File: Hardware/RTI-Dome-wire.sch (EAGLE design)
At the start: 34 parts, among them IC2 74LVC244

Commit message: Auto detect shutter presence.
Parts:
- added C5: 100nF, rti:C-EU'0805'
- added IC1: 24AA128ST, microchip:24AA128ST
- added R1, R3: 1K, rti:R-EU'0805'
- X10, X7, X9: device con-ptr500:AK500/2 -> con-ptr500:AK500/3
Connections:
- removed net 13: PCB1.13
- removed net N$6: JP4.1, PCB1.SCL1
- removed net N$8: JP4.2, PCB1.SDA1
- new net D13: PCB1.13, X8-2.KL
- new net SCL: IC1.SCL, JP4.1, PCB1.SCL1, R3.1
- new net SDA: IC1.SDA, JP4.2, PCB1.SDA1, R1.1
- net +12V: now also X11-2.KL; no longer X7-2.KL
- net 3.3V: now also C5.1, IC1.VCC, R1.2, R3.2
- net AT_PARK_PIN: now also X7-2.KL; no longer X11-1.KL
- net AT_PARK_PIN_LOOP: now also X7-3.KL; no longer X11-2.KL
- net GND: now also C5.2, IC1.A0, IC1.A1, IC1.A2, IC1.GND, X10-2.KL, X11-1.KL, X9-3.KL; no longer X10-1.KL
- net M_DIR_5V: now also X10-1.KL; no longer X9-2.KL
- net M_EN_5V: now also X9-2.KL; no longer X10-2.KL
- net M_STEP_5V: now also X10-3.KL; no longer X8-2.KL
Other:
- moved on the sheet: C1, IC2, R13, R14, R15, R16, R17, R18, R19, R4, R5, X10-1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

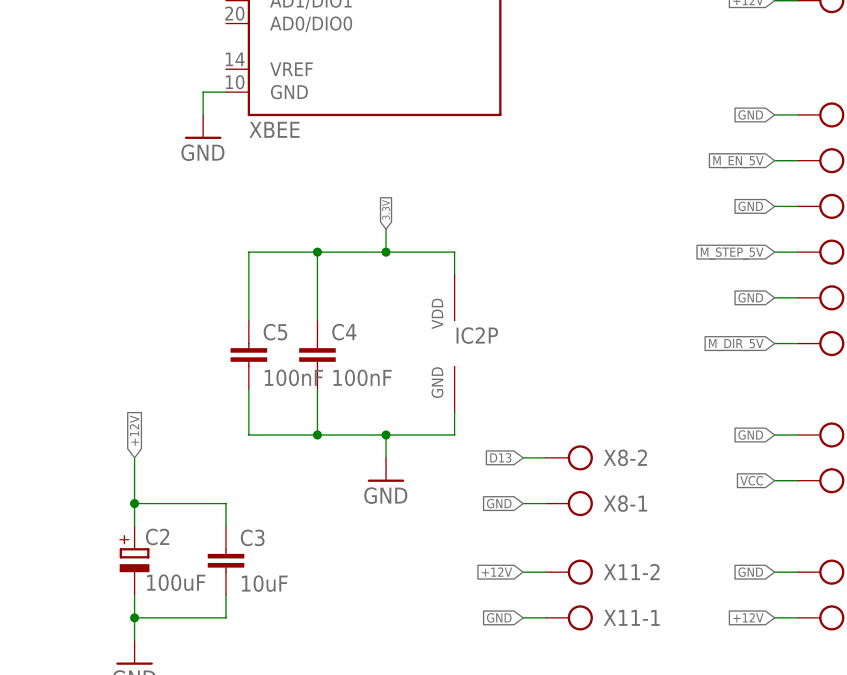
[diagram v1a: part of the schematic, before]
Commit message: Tested the ISD04 stepper controller.. needed to add 3.3V header as the pull-up on the buffer output don't bring the signal to 5V and therefore the optocoupler in the contoller doesn't do the right thing.
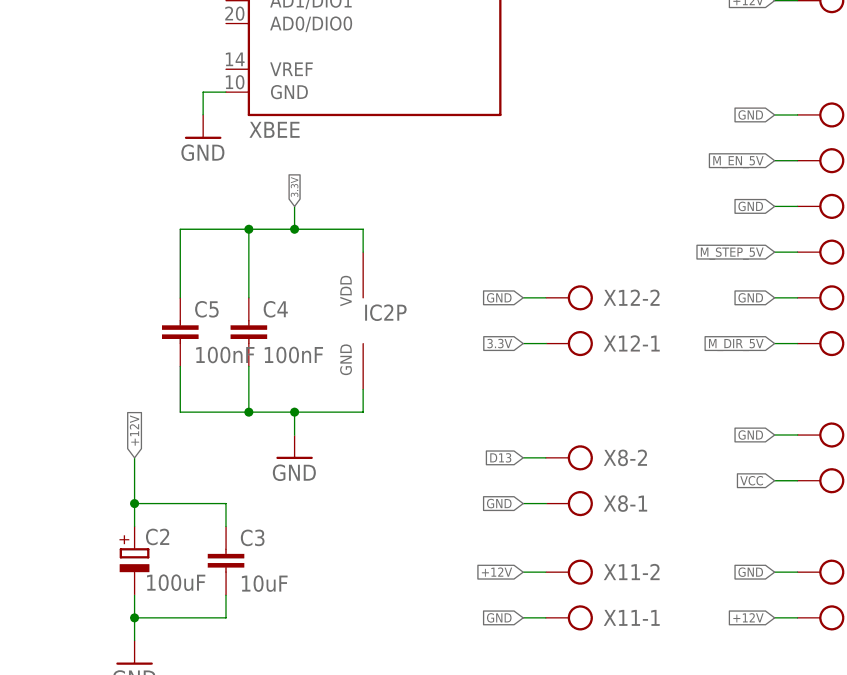
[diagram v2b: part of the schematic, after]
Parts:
- added X12: (no value), con-ptr500:AK500/2
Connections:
- net 3.3V: now also X12-1.KL
- net GND: now also X12-2.KL
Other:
- moved on the sheet: C4, C5, IC2P
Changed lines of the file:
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@@
 <part name="R3" library="rti" deviceset="R-EU" device="'0805'" value="1K"/>
 <part name="C5" library="rti" deviceset="C-EU" device="'0805'" value="100nF"/>
+<part name="X12" library="con-ptr500" deviceset="AK500/2" device=""/>
 </parts>
 <sheets>
@@
 <instance part="R8" gate="G$1" x="5.08" y="154.94" rot="R90"/>
 <instance part="R10" gate="G$1" x="5.08" y="167.64" rot="R90"/>
-<instance part="C4" gate="G$1" x="195.58" y="76.2"/>
-<instance part="IC2" gate="P" x="208.28" y="76.2" rot="R270"/>
-<instance part="GND1" gate="1" x="203.2" y="60.96"/>
+<instance part="C4" gate="G$1" x="187.96" y="78.74"/>
+<instance part="IC2" gate="P" x="198.12" y="78.74" rot="R270"/>
+<instance part="GND1" gate="1" x="193.04" y="63.5"/>
 <instance part="XB1" gate="G$1" x="200.66" y="132.08"/>
 <instance part="GND6" gate="1" x="182.88" y="99.06"/>
@@
 <instance part="R1" gate="G$1" x="73.66" y="157.48" rot="R90"/>
 <instance part="R3" gate="G$1" x="38.1" y="165.1" rot="R90"/>
-<instance part="C5" gate="G$1" x="187.96" y="76.2"/>
+<instance part="C5" gate="G$1" x="180.34" y="78.74"/>
+<instance part="X12" gate="-1" x="226.06" y="76.2" rot="R180"/>
+<instance part="X12" gate="-2" x="226.06" y="81.28" rot="R180"/>
 </instances>
 <busses>
@@
 </segment>
 <segment>
-<wire x1="195.58" y1="66.04" x2="203.2" y2="66.04" width="0.1524" layer="91"/>
-<wire x1="203.2" y1="66.04" x2="210.82" y2="66.04" width="0.1524" layer="91"/>
+<wire x1="187.96" y1="68.58" x2="193.04" y2="68.58" width="0.1524" layer="91"/>
+<wire x1="193.04" y1="68.58" x2="200.66" y2="68.58" width="0.1524" layer="91"/>
 <pinref part="IC2" gate="P" pin="GND"/>
-<wire x1="210.82" y1="68.58" x2="210.82" y2="66.04" width="0.1524" layer="91"/>
+<wire x1="200.66" y1="71.12" x2="200.66" y2="68.58" width="0.1524" layer="91"/>
 <pinref part="C4" gate="G$1" pin="2"/>
-<wire x1="195.58" y1="71.12" x2="195.58" y2="66.04" width="0.1524" layer="91"/>
-<wire x1="203.2" y1="66.04" x2="203.2" y2="63.5" width="0.1524" layer="91"/>
-<junction x="203.2" y="66.04"/>
+<wire x1="187.96" y1="73.66" x2="187.96" y2="68.58" width="0.1524" layer="91"/>
+<wire x1="193.04" y1="68.58" x2="193.04" y2="66.04" width="0.1524" layer="91"/>
+<junction x="193.04" y="68.58"/>
 <pinref part="GND1" gate="1" pin="GND"/>
 <pinref part="C5" gate="G$1" pin="2"/>
-<wire x1="195.58" y1="66.04" x2="187.96" y2="66.04" width="0.1524" layer="91"/>
-<wire x1="187.96" y1="66.04" x2="187.96" y2="71.12" width="0.1524" layer="91"/>
-<junction x="195.58" y="66.04"/>
+<wire x1="187.96" y1="68.58" x2="180.34" y2="68.58" width="0.1524" layer="91"/>
+<wire x1="180.34" y1="68.58" x2="180.34" y2="73.66" width="0.1524" layer="91"/>
+<junction x="187.96" y="68.58"/>
 </segment>
 <segment>
@@
 <junction x="60.96" y="137.16"/>
 </segment>
+<segment>
+<pinref part="X12" gate="-2" pin="KL"/>
+<wire x1="218.44" y1="81.28" x2="220.98" y2="81.28" width="0.1524" layer="91"/>
+<label x="218.44" y="81.28" size="1.016" layer="95" rot="R180" xref="yes"/>
+</segment>
 </net>
 <net name="+12V" class="1">
@@
 </segment>
 <segment>
-<wire x1="210.82" y1="86.36" x2="203.2" y2="86.36" width="0.1524" layer="91"/>
-<wire x1="203.2" y1="86.36" x2="195.58" y2="86.36" width="0.1524" layer="91"/>
+<wire x1="200.66" y1="88.9" x2="193.04" y2="88.9" width="0.1524" layer="91"/>
+<wire x1="193.04" y1="88.9" x2="187.96" y2="88.9" width="0.1524" layer="91"/>
 <pinref part="C4" gate="G$1" pin="1"/>
-<wire x1="195.58" y1="86.36" x2="195.58" y2="78.74" width="0.1524" layer="91"/>
+<wire x1="187.96" y1="88.9" x2="187.96" y2="81.28" width="0.1524" layer="91"/>
 <pinref part="IC2" gate="P" pin="VDD"/>
-<wire x1="210.82" y1="86.36" x2="210.82" y2="83.82" width="0.1524" layer="91"/>
-<wire x1="203.2" y1="86.36" x2="203.2" y2="88.9" width="0.1524" layer="91"/>
-<junction x="203.2" y="86.36"/>
-<label x="203.2" y="88.9" size="0.8128" layer="95" rot="R90" xref="yes"/>
+<wire x1="200.66" y1="88.9" x2="200.66" y2="86.36" width="0.1524" layer="91"/>
+<wire x1="193.04" y1="88.9" x2="193.04" y2="91.44" width="0.1524" layer="91"/>
+<junction x="193.04" y="88.9"/>
+<label x="193.04" y="91.44" size="0.8128" layer="95" rot="R90" xref="yes"/>
 <pinref part="C5" gate="G$1" pin="1"/>
-<wire x1="195.58" y1="86.36" x2="187.96" y2="86.36" width="0.1524" layer="91"/>
-<wire x1="187.96" y1="86.36" x2="187.96" y2="78.74" width="0.1524" layer="91"/>
-<junction x="195.58" y="86.36"/>
+<wire x1="187.96" y1="88.9" x2="180.34" y2="88.9" width="0.1524" layer="91"/>
+<wire x1="180.34" y1="88.9" x2="180.34" y2="81.28" width="0.1524" layer="91"/>
+<junction x="187.96" y="88.9"/>
 </segment>
 <segment>
@@
 <label x="73.66" y="165.1" size="1.016" layer="95" rot="R90" xref="yes"/>
 </segment>
-</net>
+<segment>
+<pinref part="X12" gate="-1" pin="KL"/>
+<wire x1="218.44" y1="76.2" x2="220.98" y2="76.2" width="0.1524" layer="91"/>
+<label x="218.44" y="76.2" size="1.016" layer="95" rot="R180" xref="yes"/>
+</segment>
+</net>

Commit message: Adding a usb-serial + usb port on SERIAL2 (pin 16 and 17)
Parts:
- added C8: 100nF, rti:C-EU'0805'
- added IC3: FT232RL, ftdichip:FT232RL
- added R11: 10K, rti:R-EU'0805'
- added R9: 4.7K, rti:R-EU'0805'
- added X13: PN61729-S, con-berg:PN61729-S
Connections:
- new net N$1: IC3.!RESET, R11.1, R9.2
- new net N$21: IC3.!DCD
- new net N$4: IC3.!CTS, IC3.!RTS
- new net N$6: C8.1, IC3.3V3OUT
- new net RX2: IC3.TXD, PCB1.17(RX2)
- new net TX2: IC3.RXD, PCB1.16(TX2)
- new net USBDM: IC3.USBDM, X13.2
- new net USBDP: IC3.USBDP, X13.3
- new net USB_VCC: R9.1, X13.1
- net 3.3V: now also IC3.VCCIO
- net GND: now also C8.2, IC3.GND, IC3.GND@1, IC3.GND@2, IC3.GND@A, R11.2, X13.4, X13.S1, X13.S2
- net VCC: now also IC3.VCC
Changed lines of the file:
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@@
 <part name="C5" library="rti" deviceset="C-EU" device="'0805'" value="100nF"/>
 <part name="X12" library="con-ptr500" deviceset="AK500/2" device=""/>
+<part name="IC3" library="ftdichip" deviceset="FT232R" device="L"/>
+<part name="GND10" library="supply1" deviceset="GND" device=""/>
+<part name="R9" library="rti" deviceset="R-EU" device="'0805'" value="4.7K"/>
+<part name="R11" library="rti" deviceset="R-EU" device="'0805'" value="10K"/>
+<part name="GND11" library="supply1" deviceset="GND" device=""/>
+<part name="X13" library="con-berg" deviceset="PN61729-S" device=""/>
+<part name="C8" library="rti" deviceset="C-EU" device="'0805'" value="100nF"/>
 </parts>
 <sheets>
@@
 <instance part="X12" gate="-1" x="226.06" y="76.2" rot="R180"/>
 <instance part="X12" gate="-2" x="226.06" y="81.28" rot="R180"/>
+<instance part="IC3" gate="1" x="340.36" y="124.46"/>
+<instance part="GND10" gate="1" x="325.12" y="86.36"/>
+<instance part="R9" gate="G$1" x="307.34" y="147.32" rot="R270"/>
+<instance part="R11" gate="G$1" x="307.34" y="132.08" rot="R270"/>
+<instance part="GND11" gate="1" x="307.34" y="121.92"/>
+<instance part="X13" gate="G$1" x="281.94" y="101.6" rot="R180"/>
+<instance part="C8" gate="G$1" x="312.42" y="101.6"/>
 </instances>
 <busses>
@@
 <label x="218.44" y="81.28" size="1.016" layer="95" rot="R180" xref="yes"/>
 </segment>
+<segment>
+<pinref part="IC3" gate="1" pin="GND@1"/>
+<wire x1="355.6" y1="101.6" x2="360.68" y2="101.6" width="0.1524" layer="91"/>
+<wire x1="360.68" y1="101.6" x2="360.68" y2="91.44" width="0.1524" layer="91"/>
+<pinref part="IC3" gate="1" pin="GND"/>
+<wire x1="355.6" y1="104.14" x2="363.22" y2="104.14" width="0.1524" layer="91"/>
+<wire x1="363.22" y1="104.14" x2="363.22" y2="93.98" width="0.1524" layer="91"/>
+<wire x1="363.22" y1="93.98" x2="360.68" y2="91.44" width="0.1524" layer="91"/>
+<pinref part="IC3" gate="1" pin="GND@2"/>
+<wire x1="355.6" y1="99.06" x2="358.14" y2="99.06" width="0.1524" layer="91"/>
+<wire x1="358.14" y1="99.06" x2="358.14" y2="93.98" width="0.1524" layer="91"/>
+<wire x1="360.68" y1="91.44" x2="358.14" y2="93.98" width="0.1524" layer="91"/>
+<junction x="360.68" y="91.44"/>
+<pinref part="IC3" gate="1" pin="GND@A"/>
+<wire x1="327.66" y1="106.68" x2="325.12" y2="106.68" width="0.1524" layer="91"/>
+<wire x1="325.12" y1="106.68" x2="325.12" y2="91.44" width="0.1524" layer="91"/>
+<wire x1="325.12" y1="91.44" x2="325.12" y2="88.9" width="0.1524" layer="91"/>
+<wire x1="360.68" y1="91.44" x2="325.12" y2="91.44" width="0.1524" layer="91"/>
+<junction x="325.12" y="91.44"/>
+<pinref part="GND10" gate="1" pin="GND"/>
+<pinref part="C8" gate="G$1" pin="2"/>
+<wire x1="325.12" y1="91.44" x2="312.42" y2="91.44" width="0.1524" layer="91"/>
+<wire x1="312.42" y1="91.44" x2="312.42" y2="96.52" width="0.1524" layer="91"/>
+</segment>
+<segment>
+<pinref part="R11" gate="G$1" pin="2"/>
+<wire x1="307.34" y1="127" x2="307.34" y2="124.46" width="0.1524" layer="91"/>
+<pinref part="GND11" gate="1" pin="GND"/>
+</segment>
+<segment>
+<pinref part="X13" gate="G$1" pin="4"/>
+<wire x1="292.1" y1="104.14" x2="289.56" y2="104.14" width="0.1524" layer="91"/>
+<label x="292.1" y="104.14" size="1.016" layer="95" xref="yes"/>
+<pinref part="X13" gate="G$1" pin="S1"/>
+<wire x1="289.56" y1="104.14" x2="287.02" y2="104.14" width="0.1524" layer="91"/>
+<wire x1="287.02" y1="104.14" x2="284.48" y2="104.14" width="0.1524" layer="91"/>
+<wire x1="281.94" y1="109.22" x2="287.02" y2="109.22" width="0.1524" layer="91"/>
+<wire x1="287.02" y1="109.22" x2="287.02" y2="104.14" width="0.1524" layer="91"/>
+<junction x="287.02" y="104.14"/>
+<pinref part="X13" gate="G$1" pin="S2"/>
+<wire x1="281.94" y1="111.76" x2="289.56" y2="111.76" width="0.1524" layer="91"/>
+<wire x1="289.56" y1="111.76" x2="289.56" y2="104.14" width="0.1524" layer="91"/>
+<junction x="289.56" y="104.14"/>
+</segment>
 </net>
 <net name="+12V" class="1">
@@
 <wire x1="218.44" y1="76.2" x2="220.98" y2="76.2" width="0.1524" layer="91"/>
 <label x="218.44" y="76.2" size="1.016" layer="95" rot="R180" xref="yes"/>
+</segment>
+<segment>
+<pinref part="IC3" gate="1" pin="VCCIO"/>
+<wire x1="327.66" y1="144.78" x2="314.96" y2="144.78" width="0.1524" layer="91"/>
+<wire x1="314.96" y1="144.78" x2="314.96" y2="149.86" width="0.1524" layer="91"/>
+<label x="314.96" y="149.86" size="1.016" layer="95" rot="R90" xref="yes"/>
 </segment>
 </net>
@@
 <pinref part="X6" gate="-1" pin="KL"/>
 </segment>
+<segment>
+<pinref part="IC3" gate="1" pin="VCC"/>
+<wire x1="327.66" y1="147.32" x2="320.04" y2="147.32" width="0.1524" layer="91"/>
+<wire x1="320.04" y1="147.32" x2="320.04" y2="149.86" width="0.1524" layer="91"/>
+<label x="320.04" y="149.86" size="1.016" layer="95" rot="R90" xref="yes"/>
+</segment>
 </net>
 <net name="N$2" class="0">
@@
 </segment>
 </net>
+<net name="N$1" class="0">
+<segment>
+<pinref part="R9" gate="G$1" pin="2"/>
+<pinref part="R11" gate="G$1" pin="1"/>
+<wire x1="307.34" y1="142.24" x2="307.34" y2="139.7" width="0.1524" layer="91"/>
+<pinref part="IC3" gate="1" pin="!RESET"/>
+<wire x1="307.34" y1="139.7" x2="307.34" y2="137.16" width="0.1524" layer="91"/>
+<wire x1="327.66" y1="139.7" x2="307.34" y2="139.7" width="0.1524" layer="91"/>
+<junction x="307.34" y="139.7"/>
+</segment>
+</net>
+<net name="USB_VCC" class="0">
+<segment>
+<pinref part="X13" gate="G$1" pin="1"/>
+<wire x1="287.02" y1="96.52" x2="284.48" y2="96.52" width="0.1524" layer="91"/>
+<label x="287.02" y="96.52" size="1.016" layer="95" xref="yes"/>
+</segment>
+<segment>
+<pinref part="R9" gate="G$1" pin="1"/>
+<wire x1="299.72" y1="154.94" x2="307.34" y2="154.94" width="0.1524" layer="91"/>
+<wire x1="307.34" y1="154.94" x2="307.34" y2="152.4" width="0.1524" layer="91"/>
+<label x="299.72" y="154.94" size="1.016" layer="95" rot="R180" xref="yes"/>
+</segment>
+</net>
+<net name="USBDP" class="0">
+<segment>
+<pinref part="IC3" gate="1" pin="USBDP"/>
+<wire x1="325.12" y1="114.3" x2="327.66" y2="114.3" width="0.1524" layer="91"/>
+<label x="325.12" y="114.3" size="1.016" layer="95" rot="R180" xref="yes"/>
+</segment>
+<segment>
+<pinref part="X13" gate="G$1" pin="3"/>
+<wire x1="287.02" y1="101.6" x2="284.48" y2="101.6" width="0.1524" layer="91"/>
+<label x="287.02" y="101.6" size="1.016" layer="95" xref="yes"/>
+</segment>
+</net>
+<net name="USBDM" class="0">
+<segment>
+<pinref part="IC3" gate="1" pin="USBDM"/>
+<wire x1="325.12" y1="111.76" x2="327.66" y2="111.76" width="0.1524" layer="91"/>
+<label x="325.12" y="111.76" size="1.016" layer="95" rot="R180" xref="yes"/>
+</segment>
+<segment>
+<pinref part="X13" gate="G$1" pin="2"/>
+<wire x1="287.02" y1="99.06" x2="284.48" y2="99.06" width="0.1524" layer="91"/>
+<label x="287.02" y="99.06" size="1.016" layer="95" xref="yes"/>
+</segment>
+</net>
+<net name="N$6" class="0">
+<segment>
+<pinref part="IC3" gate="1" pin="3V3OUT"/>
+<wire x1="327.66" y1="119.38" x2="312.42" y2="119.38" width="0.1524" layer="91"/>
+<wire x1="312.42" y1="119.38" x2="312.42" y2="104.14" width="0.1524" layer="91"/>
+<pinref part="C8" gate="G$1" pin="1"/>
+</segment>
+</net>
+<net name="N$21" class="0">
+<segment>
+<pinref part="IC3" gate="1" pin="!DCD"/>
+<wire x1="358.14" y1="132.08" x2="355.6" y2="132.08" width="0.1524" layer="91"/>
+</segment>
+</net>
+<net name="N$4" class="0">
+<segment>
+<pinref part="IC3" gate="1" pin="!RTS"/>
+<wire x1="355.6" y1="142.24" x2="358.14" y2="142.24" width="0.1524" layer="91"/>
+<wire x1="358.14" y1="142.24" x2="358.14" y2="139.7" width="0.1524" layer="91"/>
+<pinref part="IC3" gate="1" pin="!CTS"/>
+<wire x1="358.14" y1="139.7" x2="355.6" y2="139.7" width="0.1524" layer="91"/>
+</segment>
+</net>
+<net name="RX2" class="0">
+<segment>
+<pinref part="PCB1" gate="G$1" pin="17(RX2)"/>
+<wire x1="137.16" y1="25.4" x2="134.62" y2="25.4" width="0.1524" layer="91"/>
+<label x="137.16" y="25.4" size="1.016" layer="95" xref="yes"/>
+</segment>
+<segment>
+<pinref part="IC3" gate="1" pin="TXD"/>
+<wire x1="358.14" y1="147.32" x2="355.6" y2="147.32" width="0.1524" layer="91"/>
+<label x="358.14" y="147.32" size="0.8128" layer="95" xref="yes"/>
+</segment>
+</net>
+<net name="TX2" class="0">
+<segment>
+<pinref part="PCB1" gate="G$1" pin="16(TX2)"/>
+<wire x1="137.16" y1="27.94" x2="134.62" y2="27.94" width="0.1524" layer="91"/>
+<label x="137.16" y="27.94" size="1.016" layer="95" xref="yes"/>
+</segment>
+<segment>
+<pinref part="IC3" gate="1" pin="RXD"/>
+<wire x1="358.14" y1="144.78" x2="355.6" y2="144.78" width="0.1524" layer="91"/>
+<label x="358.14" y="144.78" size="0.8128" layer="95" xref="yes"/>
+</segment>
+</net>

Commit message: Remove I2C 2 pin header as we now have the eeprom on the board.
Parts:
- removed JP4: (no value), jumper:JP1E
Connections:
- net SCL: no longer JP4.1
- net SDA: no longer JP4.2
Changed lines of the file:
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@@
 <part name="R5" library="rti" deviceset="R-EU" device="'0805'" value="100"/>
 <part name="FRAME1" library="frames" deviceset="DINA4_L" device=""/>
-<part name="JP4" library="jumper" deviceset="JP1E" device=""/>
 <part name="U$4" library="rti" deviceset="RTI-LOGO" device="_BIG" value="RTI-LOGO_BIG"/>
 <part name="C2" library="rti" deviceset="CPOL-EU" device="" value="100uF"/>
@@
 <instance part="FRAME1" gate="G$1" x="0" y="0"/>
 <instance part="FRAME1" gate="G$2" x="162.56" y="0"/>
-<instance part="JP4" gate="A" x="147.32" y="96.52"/>
 <instance part="U$4" gate="G$1" x="167.64" y="27.94"/>
 <instance part="C2" gate="G$1" x="175.26" y="53.34"/>
@@
 </segment>
 <segment>
-<pinref part="JP4" gate="A" pin="2"/>
 <wire x1="134.62" y1="86.36" x2="149.86" y2="86.36" width="0.1524" layer="91"/>
-<wire x1="149.86" y1="86.36" x2="149.86" y2="93.98" width="0.1524" layer="91"/>
 <pinref part="PCB1" gate="G$1" pin="SDA1"/>
 <wire x1="149.86" y1="86.36" x2="154.94" y2="86.36" width="0.1524" layer="91"/>
-<junction x="149.86" y="86.36"/>
 <label x="154.94" y="86.36" size="1.016" layer="95" xref="yes"/>
 </segment>
@@
 </segment>
 <segment>
-<pinref part="JP4" gate="A" pin="1"/>
 <wire x1="134.62" y1="88.9" x2="147.32" y2="88.9" width="0.1524" layer="91"/>
-<wire x1="147.32" y1="88.9" x2="147.32" y2="93.98" width="0.1524" layer="91"/>
 <pinref part="PCB1" gate="G$1" pin="SCL1"/>
 <wire x1="147.32" y1="88.9" x2="154.94" y2="88.9" width="0.1524" layer="91"/>
-<junction x="147.32" y="88.9"/>
 <label x="154.94" y="88.9" size="1.016" layer="95" xref="yes"/>
 </segment>
